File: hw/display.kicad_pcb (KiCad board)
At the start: 2 copper layers, 87.3 x 60.3 mm, 62 parts, among them J1 AMPSEAL_8_POS_776275-1, J101 HEADER_MOLEX_54104-4031, J2 ARM_JTAG_SWD_HEADER_10_PINSMD, J4 HEADER_MOLEX_52207-0433, U1 MCP2551_SOIC8, U101 MOSFET-N_2N7002W, U102 AL8805W5-7_LED_DRIVER, U2 ALLIANCE_AS4C4M16SA_TSOP_II, U3 WINDBOND_W25Q32FV_SOIC8_W, U4 LPC1785FBD208_551QFP50, X1 XTAL_7A-20.000MAAJ-T, X101 XTAL_ABS25-32.768KHZ-T, X3 BUZZER_PKM13EPYH4002-B0

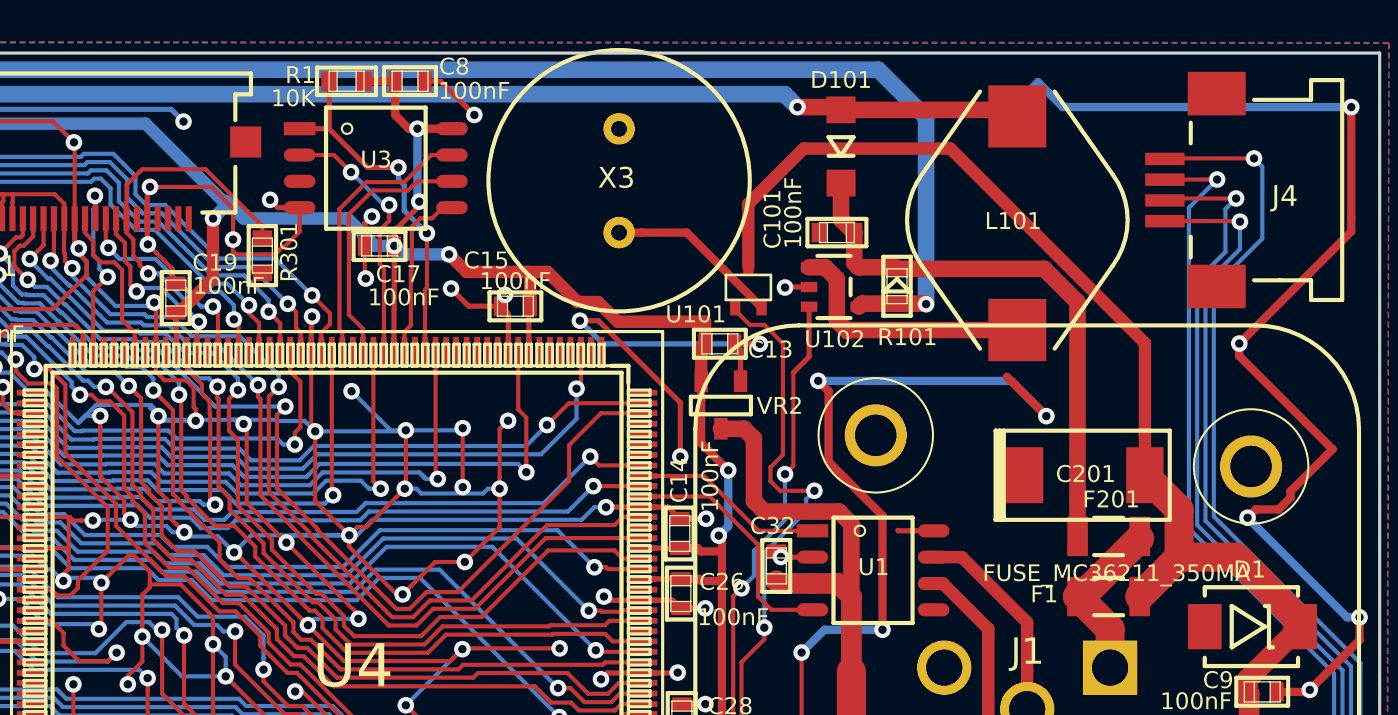
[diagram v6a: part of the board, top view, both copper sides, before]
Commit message: hw version 1.6.0
* LCD backlight remains off while booting
* BUZZER amplifying MOSFET circuit changed to low side driving
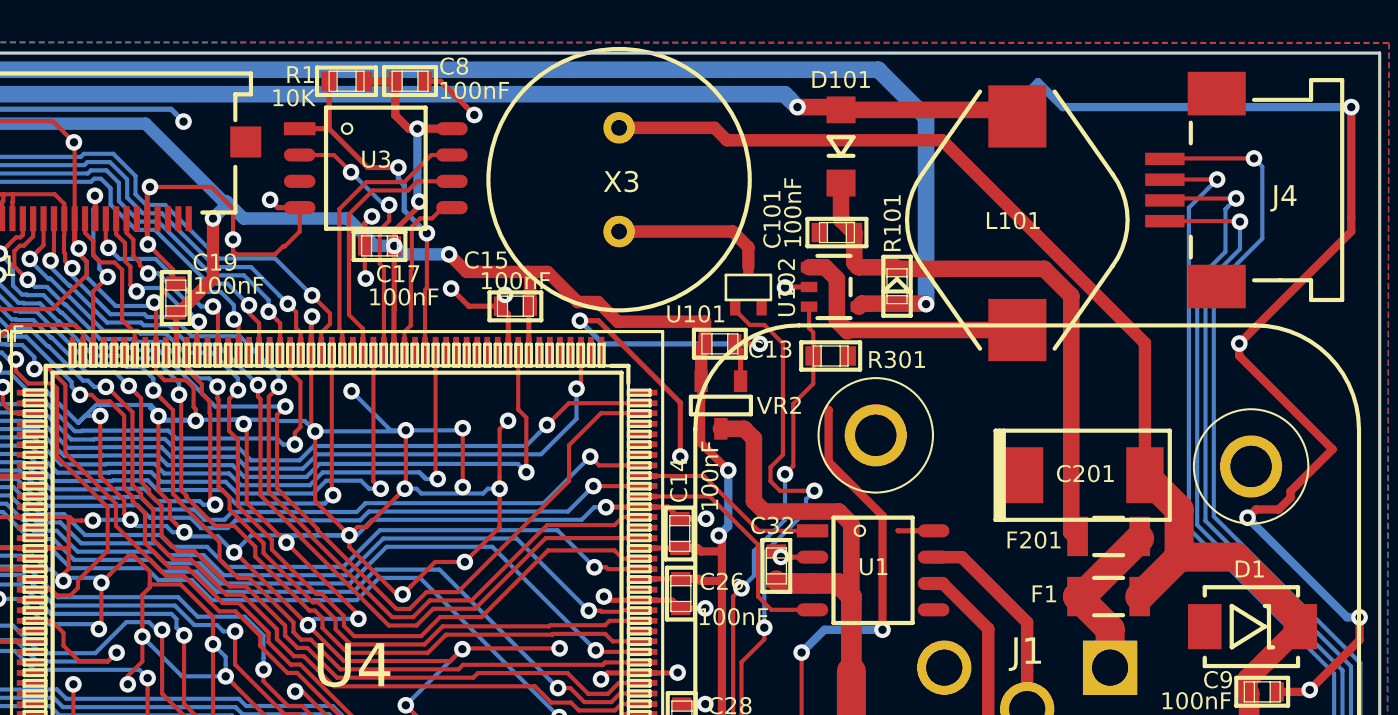
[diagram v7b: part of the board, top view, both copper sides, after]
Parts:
- moved R301 27.8 mm to (148.6, 71.5), turned to 180 degrees
- turned X3 to 270 degrees
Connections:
- R301 pad 2: /DE -> /BACKLIGHT
- U101 pad M: VDD -> Net-(U101-PadM)
- U101 pad R: Net-(U101-PadR) -> GND
- X3 pad 1: Net-(U101-PadR) -> VDD
- X3 pad 2: GND -> Net-(U101-PadM)
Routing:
- net GND: track 907.0 -> 891.0 mm, vias 147 -> 145
- net /DE: track 19.4 -> 9.16 mm
- net Net-(U101-PadR): track 8.41 -> 0.00 mm
- net Net-(U101-PadM): track 0.00 -> 7.49 mm
- net VDD: track 54.4 -> 56.9 mm

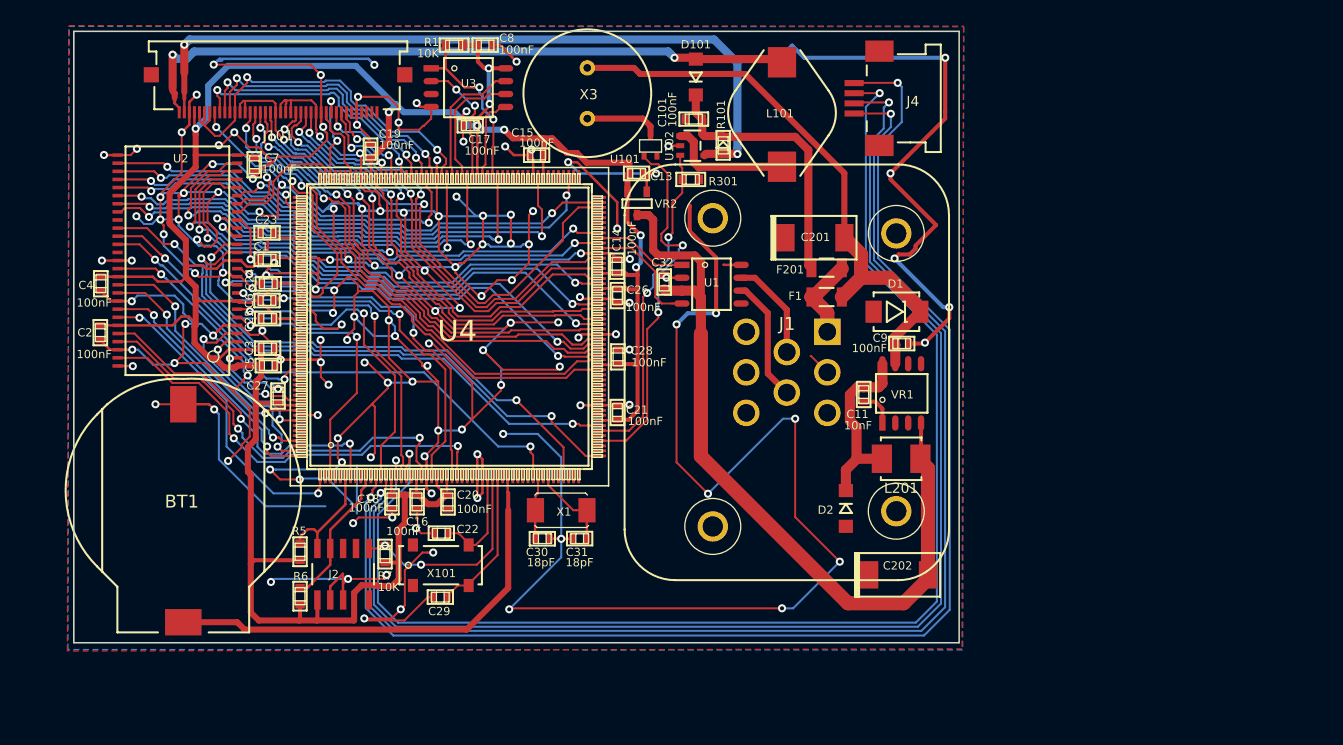
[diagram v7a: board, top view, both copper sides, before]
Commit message: porting uv0a_hds pcb to uw_display
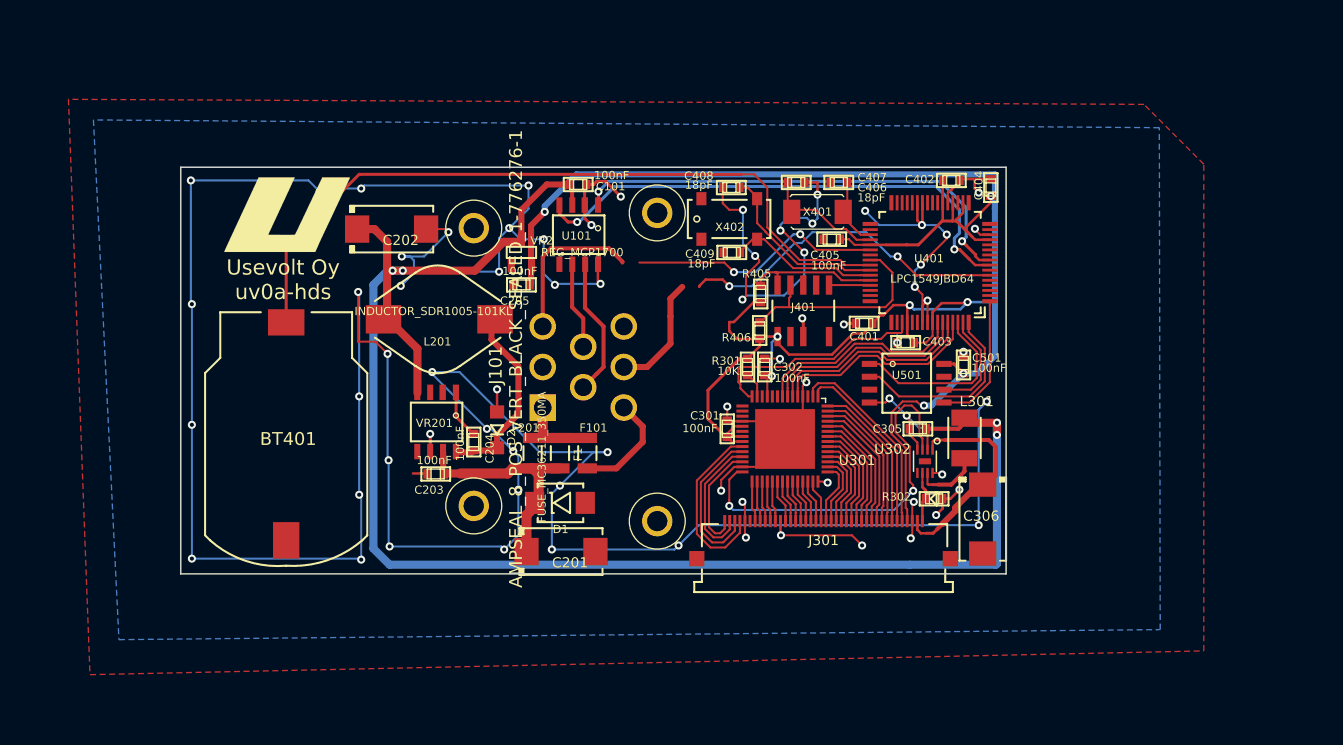
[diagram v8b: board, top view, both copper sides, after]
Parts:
- removed BT1: BATTERY_HOLDER_CH7410-2032LFSMD, usevolt:usevolt-BATTERY_HOLDER_CH7410-2032LF
- removed C1, C13, C14, C15, C16, C17, C18, C19, C2, C20, C21, C23, C24, C25, C26, C27, C28, C3, C32, C4, C5, C6, C7, C8, C9: 100nF, kemet:Kemet-CAPC1608X85N
- removed C11: 10nF, kemet:Kemet-CAPC1608X85N
- removed C22, C29: 12pF, kemet:Kemet-CAPC1608X85N
- removed C30, C31: 18pF, kemet:Kemet-CAPC1608X85N
- removed D101: DIODE_RS07J-GS18, usevolt:DO219AB
- removed J1: AMPSEAL_8_POS_776275-1, usevolt:AMPSEAL_8_POS_776275-1
- removed J2: ARM_JTAG_SWD_HEADER_10_PINSMD, usevolt:usevolt-ARM_10_PIN_JTAG_SWD_CONNECTOR
- removed J4: HEADER_MOLEX_52207-0433, usevolt:HEADER_MOLEX_52207-0433
- removed L101: INDUCTOR_SDR1005-101KL, usevolt:INDUCTOR_BOURNS_10X13X5MM
- removed R1, R5, R6, R7: 10K, multicomp:Multicomp-RESC1608X60N
- removed R101: R_0.33OHM, usevolt:0603
- removed U1: MCP2551_SOIC8, usevolt:SOIC8
- removed U102: AL8805W5-7_LED_DRIVER, usevolt:SOT-25
- removed U2: ALLIANCE_AS4C4M16SA_TSOP_II, usevolt:TSOP_II_54_PIN
- removed U3: WINDBOND_W25Q32FV_SOIC8_W, usevolt:SOIC8_W
- removed U4: LPC1785FBD208_551QFP50, usevolt:QFP208
- removed VR1: LM2671SOIC8, usevolt:SOIC8
- removed X1: XTAL_7A-20.000MAAJ-T, usevolt:XTAL_7A-20.000MAJ
- removed X101: XTAL_ABS25-32.768KHZ-T, usevolt:XTAL_32.768KHZ-T
- removed X3: BUZZER_PKM13EPYH4002-B0, usevolt:BUZZER_PKM13EPYH4002-B0
- added BT401: BATTERY_HOLDER_CH7410-2032LFSMD, usevolt:BATTERY_HOLDER_CH7410-2032LF, F.Cu at (108.7, 107.1)
- added C203: 100nF, kemet:0603, F.Cu at (123.5, 100.5)
- added C204: 100nF, kemet:0603, F.Cu at (127.2, 97.4)
- added C205: 100nF, kemet:0603, F.Cu at (131.9, 81.9)
- added C301: 100nF, kemet:0603, F.Cu at (152.2, 96.1)
- added C302: 100nF, kemet:0603, F.Cu at (155.9, 90.0)
- added C305: 100nF, kemet:0603, F.Cu at (171.0, 96.1)
- added C306: T491D226K035AT, kemet:7343, F.Cu at (177.4, 105.0)
- added C401: 100nF, kemet:0603, F.Cu at (165.7, 85.7)
- added C402: 100nF, kemet:0603, F.Cu at (174.3, 71.6)
- added C403: 100nF, kemet:0603, F.Cu at (169.8, 87.6)
- added C404: 100nF, kemet:0603, F.Cu at (178.2, 72.3)
- added C405: 100nF, kemet:0603, F.Cu at (162.5, 77.4)
- added C406: 18pF, kemet:0603, F.Cu at (163.2, 71.8)
- added C407: 18pF, kemet:0603, F.Cu at (159.0, 71.8)
- added C408: 18pF, kemet:0603, F.Cu at (152.6, 72.3)
- added C409: 18pF, kemet:0603, F.Cu at (152.7, 78.7)
- added C501: 100nF, kemet:0603, F.Cu at (175.5, 89.8)
- added F101: FUSE_MC36211_350MA, usevolt:FUSE_MC36211, F.Cu at (138.4, 98.5)
- added G***: LOGO, usevolt:uv_logo, F.Cu at (108.8, 75.0)
- added J301: HEADER_MOLEX_54104-4031, usevolt:HEADER_MOLEX_54104-4031, F.Cu at (161.7, 107.7)
- added J401: ARM_JTAG_SWD_HEADER_10_PINSMD, usevolt:ARM_10_PIN_JTAG_SWD_CONNECTOR, F.Cu at (157.2, 85.7)
- added L301: IND_744045210, usevolt:IND_744045210, F.Cu at (175.6, 97.0)
- added R302: R_2OHM, usevolt:0603, F.Cu at (172.6, 103.0)
- added R405: 10K, multicomp:0603, F.Cu at (155.5, 82.8)
- added R406: 10K, multicomp:0603, F.Cu at (155.4, 86.4)
- added U301: FT812, usevolt:QFN-56, F.Cu at (157.9, 97.1)
- added U302: LED_DRIVER_MIC2289, usevolt:MLF_8, F.Cu at (171.7, 99.3)
- added U401: LPC1549JBD64, usevolt:QFP64, F.Cu at (172.2, 79.7)
- added U501: WINDBOND_W25Q128JVSIQ_SOIC8_W, usevolt:SOIC8_W, F.Cu at (169.9, 91.6)
- added VR201: LM2671SOIC8, usevolt:SOIC8, F.Cu at (123.5, 95.4)
- added X401: XTAL_7A-12.000MAAJ-T, usevolt:XTAL_7A-20.000MAJ, F.Cu at (161.1, 74.7)
- added X402: XTAL_ABS25-32.768KHZ-T, usevolt:XTAL_32.768KHZ-T, F.Cu at (152.4, 75.4)
- J101: value HEADER_MOLEX_54104-4031 -> AMPSEAL_8_POS_VERT_BLACK_SEALED_1-776276-1; footprint usevolt:HEADER_MOLEX_54104-4031 -> usevolt:AMPSEAL_8_POS_776275-1
- L201: value IND_744045210 -> INDUCTOR_SDR1005-101KL; footprint usevolt:IND_744045210 -> usevolt:INDUCTOR_BOURNS_10X13X5MM
- U101: value MOSFET-N_2N7002W -> MCP2551_SOIC8; footprint usevolt:SOT323 -> usevolt:SOIC8
- moved C202 60.5 mm to (119.1, 76.4), turned to 0 degrees
- moved L201 47.6 mm to (123.8, 85.3), turned to 180 degrees
- moved J101 40.9 mm to (138.0, 90.0), turned to 90 degrees
- moved C201 39.8 mm to (135.8, 108.2), turned to 0 degrees
- moved D1 38.2 mm to (135.7, 103.4), turned to 180 degrees
- moved D2 35.3 mm to (129.5, 96.2), turned to 270 degrees
- moved F201 34.3 mm to (133.0, 98.5), turned to 270 degrees
- moved F1 30.5 mm to (135.7, 98.5), turned to 90 degrees
- moved R301 19.3 mm to (154.2, 90.0), turned to 90 degrees
- moved C101 13.1 mm to (137.5, 72.0)
- moved VR2 12.4 mm to (131.9, 78.7), turned to 0 degrees
- moved U101 11.3 mm to (137.6, 77.0), turned to 270 degrees
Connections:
- C101 pad 1: GND -> +5V
- C101 pad 2: /pwr_supply_sheet/VLCD -> GND
- D2 pad P$2: Net-(C11-Pad2) -> Net-(C204-Pad2)
- F1 pad P$1: /pwr_supply_sheet/VIN -> VDD
- F201 pad P$1: /pwr_supply_sheet/VIN -> VDD
- F201 pad P$2: /pwr_supply_sheet/VLCD -> (no net)
- J101 pad 1: /BCKL- -> VDD
- J101 pad 10: /R2 -> (no net)
- J101 pad 11: /R3 -> (no net)
- J101 pad 12: /R4 -> (no net)
- J101 pad 2: /BCKL+ -> GND
- J101 pad 3: GND -> (no net)
- J101 pad 4: +3V3 -> /CANH
- J101 pad 5: /R4 -> /CANL
- J101 pad 6: /R4 -> Net-(F101-PadP$1)
- J101 pad 7: /R4 -> (no net)
- J101 pad 8: /R0 -> (no net)
- J101 pad 9: /R1 -> (no net)
- R301 pad 1: GND -> Net-(R301-Pad1)
- R301 pad 2: /BACKLIGHT -> +3V3
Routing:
- net GND: track 891.0 -> 472.4 mm, vias 145 -> 70
- net /lpc1785_sheet/LCD_Y_T: track 133.6 -> 0.00 mm, vias 2 -> 0
- net /lpc1785_sheet/LCD_X_R: track 131.2 -> 0.00 mm, vias 2 -> 0
- net /lpc1785_sheet/LCD_Y_B: track 131.0 -> 0.00 mm, vias 2 -> 0
- net /lpc1785_sheet/LCD_X_L: track 128.1 -> 0.00 mm, vias 2 -> 0
- net +3V3: track 297.5 -> 195.7 mm
- net +5V: track 78.4 -> 165.2 mm, vias 0 -> 4
- net /BCKL+: track 74.7 -> 0.00 mm, vias 2 -> 0
- net Net-(BT401-Pad+): track 0.00 -> 74.0 mm
- net /lpc1549/CAN_RX: track 0.00 -> 71.3 mm, vias 0 -> 2
- net (no net): track 0.00 -> 69.5 mm, vias 0 -> 4
- net /BCKL-: track 67.0 -> 0.00 mm, vias 2 -> 0
- net /lpc1549/CAN_TX: track 0.00 -> 65.5 mm, vias 0 -> 2
- net /lpc1785_sheet/EMC_CKE: track 58.8 -> 0.00 mm, vias 2 -> 0
- net /lpc1785_sheet/EMC_CLK: track 55.5 -> 0.00 mm, vias 2 -> 0
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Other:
- board size 87.3 x 60.3 mm -> 81.4 x 40.1 mm
- rule trace_min: 0.2 -> 0
- board text added: "Usevolt Oy uv0a-hds"
